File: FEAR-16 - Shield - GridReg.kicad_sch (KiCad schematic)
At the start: 8 parts, among them J1 Channel-In, J101 Supply, J102 Signals, J103 Channel-In

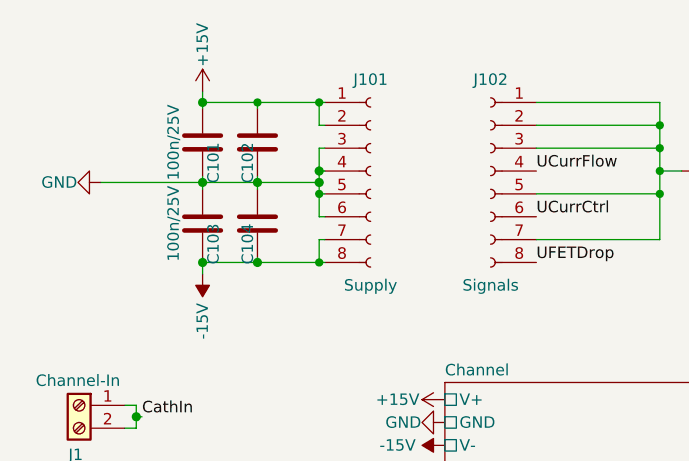
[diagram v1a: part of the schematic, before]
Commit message: Added comments on UFET feedback loop
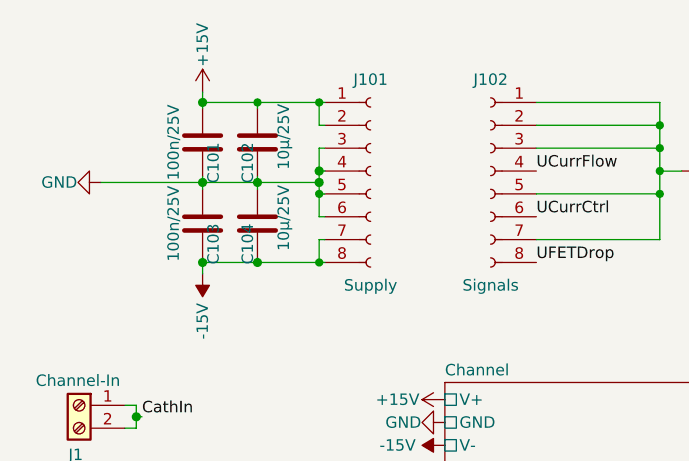
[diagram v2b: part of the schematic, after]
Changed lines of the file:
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@@
 					(size 1.27 1.27)
 				)
-				(hide yes)
 			)
 		)
@@
 					(size 1.27 1.27)
 				)
-				(hide yes)
-			)
-		)
+			)
+		)
